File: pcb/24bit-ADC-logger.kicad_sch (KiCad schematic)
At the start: 14 parts

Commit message: feat: fill schematic title block
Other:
- company: (none) -> SA6MBO
- title: (none) -> 24bit ADC logger
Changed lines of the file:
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@@
 (kicad_sch (version 20211123) (generator eeschema)
   (paper "A4")
+  (title_block
+    (title "24bit ADC logger")
+    (date "%%date%%")
+    (rev "%%version%%")
+    (company "SA6MBO")
+  )
   (junction (at 187.96 36.83) (diameter 0) (color 0 0 0 0)
   )

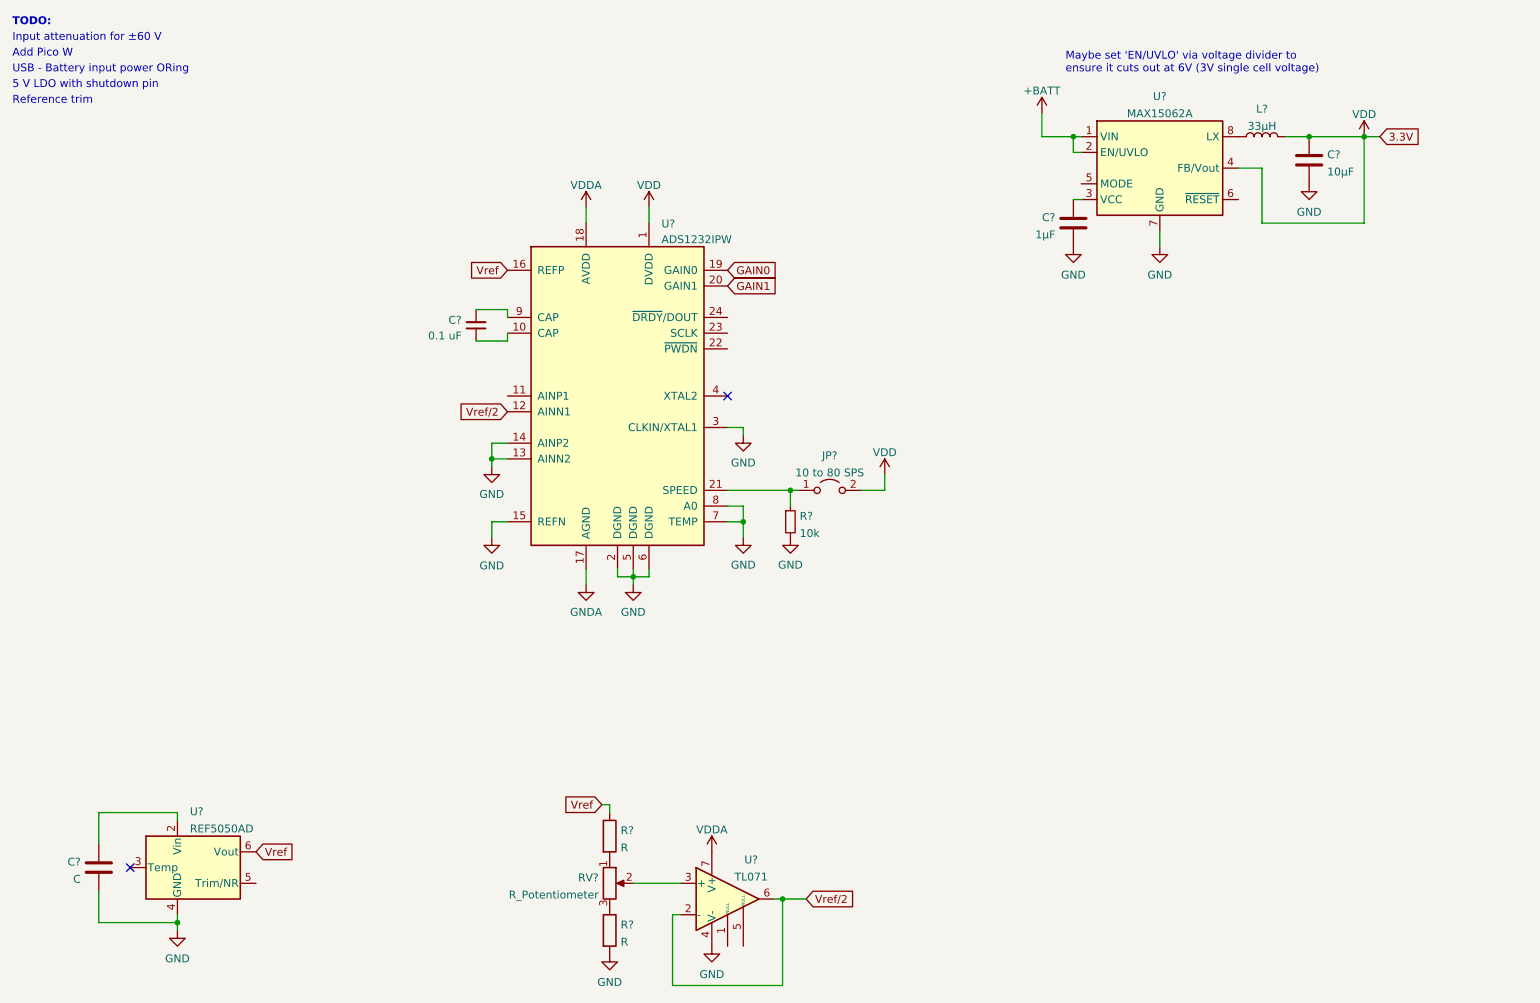
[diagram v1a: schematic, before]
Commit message: feat(sch): add battery and 5V regulator
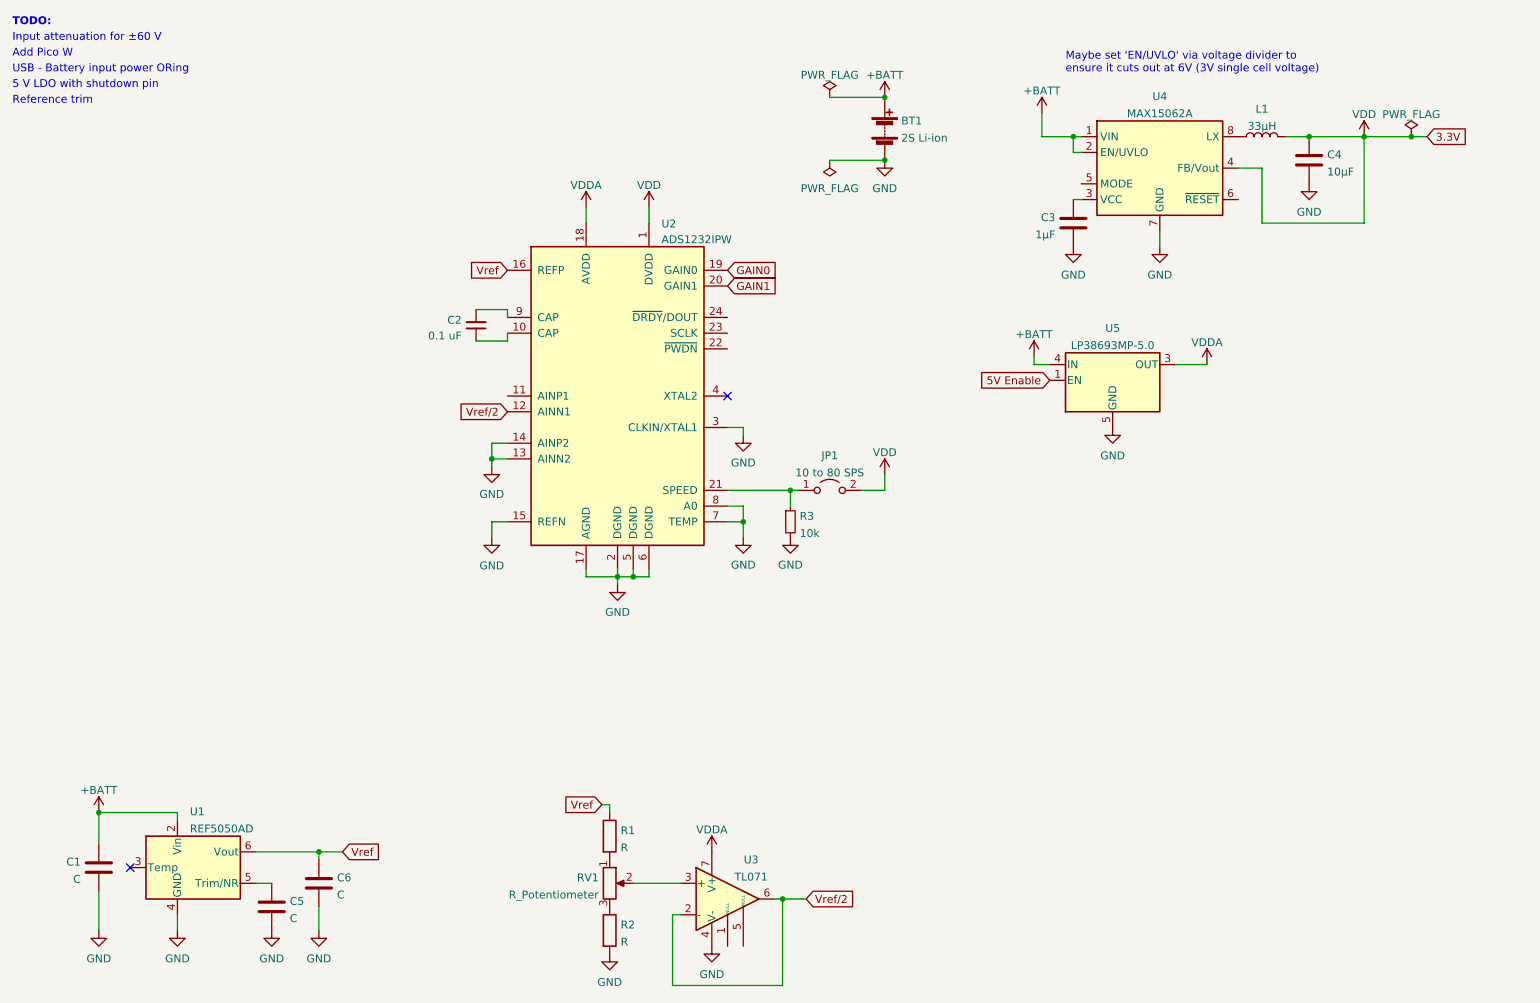
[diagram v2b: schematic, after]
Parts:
- added BT1: 2S Li-ion, symbol Device:Battery
- added C5, C6: C, symbol Device:C
- added U5: LP38693MP-5.0, Package_TO_SOT_SMD:SOT-223-5, symbol Regulator_Linear:LP38693MP-5.0
- gave numbers to parts that had none: 14
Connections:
- net GNDA is gone; now on net GND: U2.17 (AGND)
- net +BATT: now also C1.1, U1.2 (Vin), BT1.1 (+), U5.4 (IN)
- net GND: now also BT1.2 (-), C5.2, C6.2, U5.5 (GND)
- net VDDA: now also U5.3 (OUT)
- net Vref: now also C6.1
- net at U1.5 (Trim/NR): now also C5.1
- new net 5V Enable: U5.1 (EN)

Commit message: feat: add Pico W to schematic
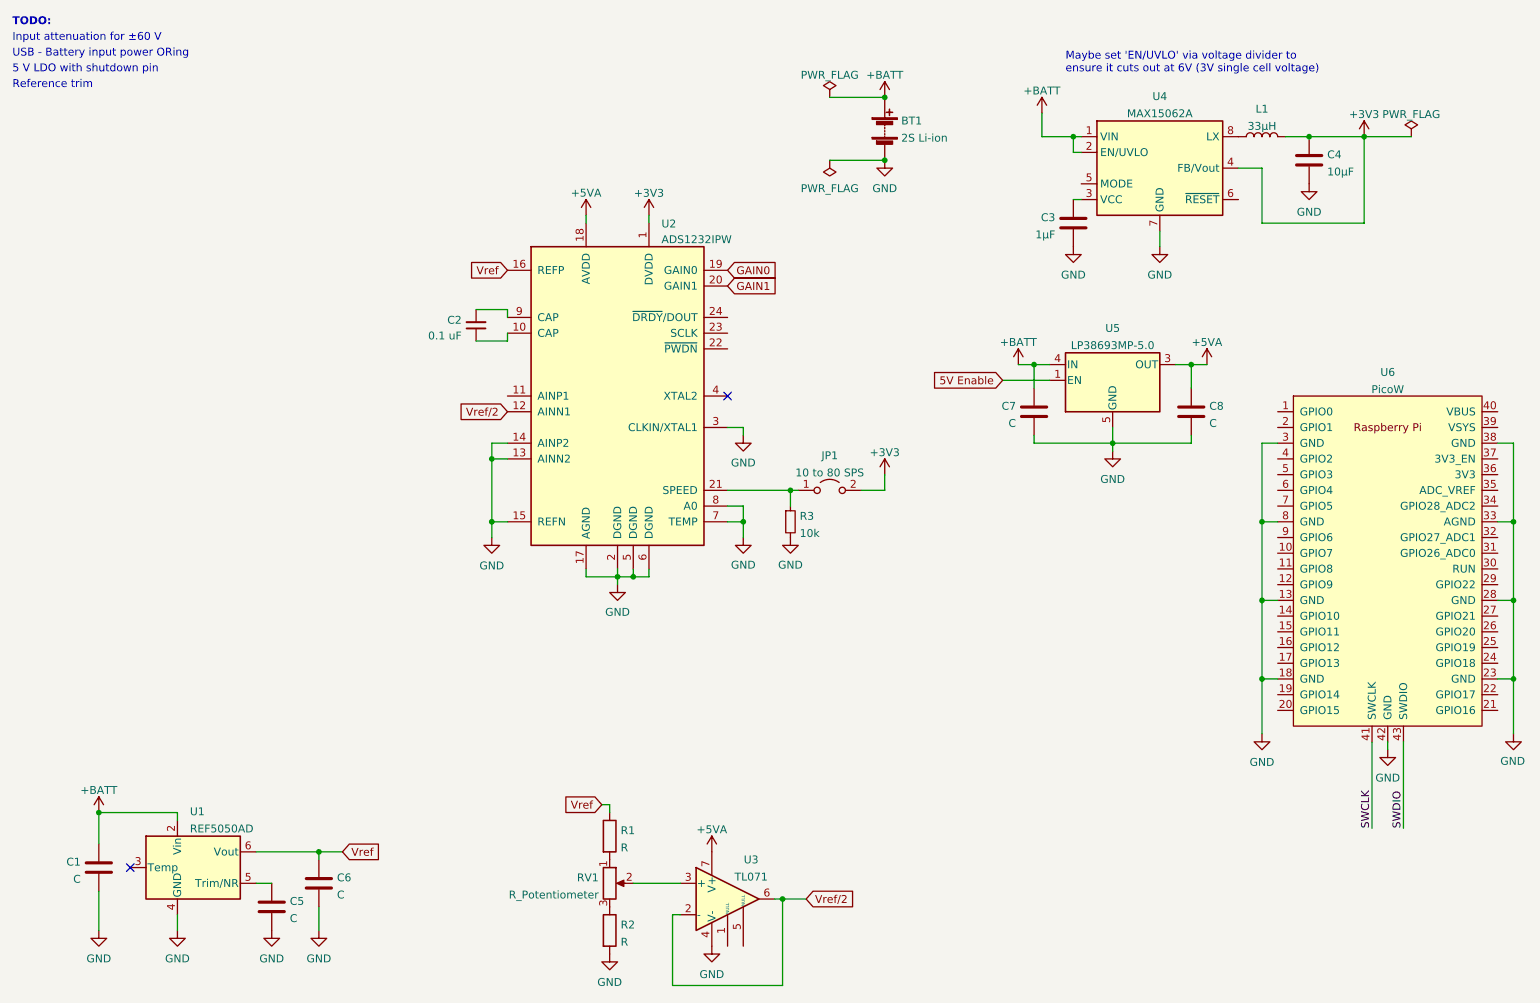
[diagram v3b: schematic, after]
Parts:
- added C7, C8: C, symbol Device:C
- added U6: PicoW, RPi_Pico:RPi_PicoW_SMD_TH, symbol RPi_Pico:PicoW
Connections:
- net +BATT: now also C7.1
- net GND: now also C7.2, C8.2, U6.13 (GND), U6.18 (GND), U6.23 (GND), U6.28 (GND), U6.3 (GND), U6.33 (AGND), U6.38 (GND), U6.42 (GND), U6.8 (GND)
- net VDD renamed +3V3
- net VDDA renamed +5VA
- net +5VA: now also C8.1
- new net SWCLK: U6.41 (SWCLK)
- new net SWDIO: U6.43 (SWDIO)
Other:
- note removed: "Add Pico W"

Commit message: test: set capacitor value to trigger CI review diff
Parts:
- C7, C8: value C -> 1uF
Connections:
- net +BATT: now also C7.2; no longer C7.1
- net GND: now also C7.1; no longer C7.2
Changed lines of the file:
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@@
     (pin "1")
   )
-  (symbol (lib_id "Device:C") (at 181.61 81.28 0) (mirror y) (unit 1)
-    (in_bom yes) (on_board yes) (fields_autoplaced)
-    (property "Reference" "C7" (id 0) (at 178.689 80.3715 0)
-      (effects (font (size 1.27 1.27)) (justify left))
-    )
-    (property "Value" "C" (id 1) (at 178.689 83.1466 0)
-      (effects (font (size 1.27 1.27)) (justify left))
-    )
-    (property "Footprint" "" (id 2) (at 180.6448 85.09 0)
+  (symbol (lib_id "Device:C") (at 181.61 81.28 0) (mirror x) (unit 1)
+    (in_bom yes) (on_board yes) (fields_autoplaced)
+    (property "Reference" "C7" (id 0) (at 178.6891 80.3715 0)
+      (effects (font (size 1.27 1.27)) (justify right))
+    )
+    (property "Value" "1uF" (id 1) (at 178.6891 83.1466 0)
+      (effects (font (size 1.27 1.27)) (justify right))
+    )
+    (property "Footprint" "" (id 2) (at 182.5752 77.47 0)
       (effects (font (size 1.27 1.27)) hide)
     )
@@
       (effects (font (size 1.27 1.27)) (justify left))
     )
-    (property "Value" "C" (id 1) (at 209.931 83.1466 0)
+    (property "Value" "1uF" (id 1) (at 209.931 83.1466 0)
       (effects (font (size 1.27 1.27)) (justify left))
     )
@@
     )
     (path "/acfc6b98-d623-44b3-b584-08e60815184f"
-      (reference "C7") (unit 1) (value "C") (footprint "")
+      (reference "C7") (unit 1) (value "1uF") (footprint "")
     )
     (path "/e08d6b8a-fd25-43ef-818b-d3ae6a475169"
-      (reference "C8") (unit 1) (value "C") (footprint "")
+      (reference "C8") (unit 1) (value "1uF") (footprint "")
     )
     (path "/5d483a2b-4b6d-4697-8bf4-fa10b54b0f95"

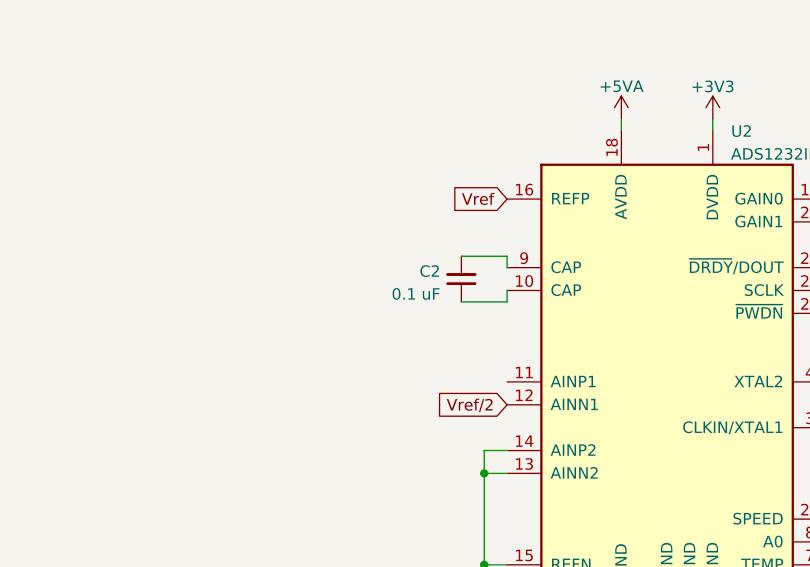
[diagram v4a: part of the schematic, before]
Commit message: ci(kibot): change commit reference for diff to HEAD~
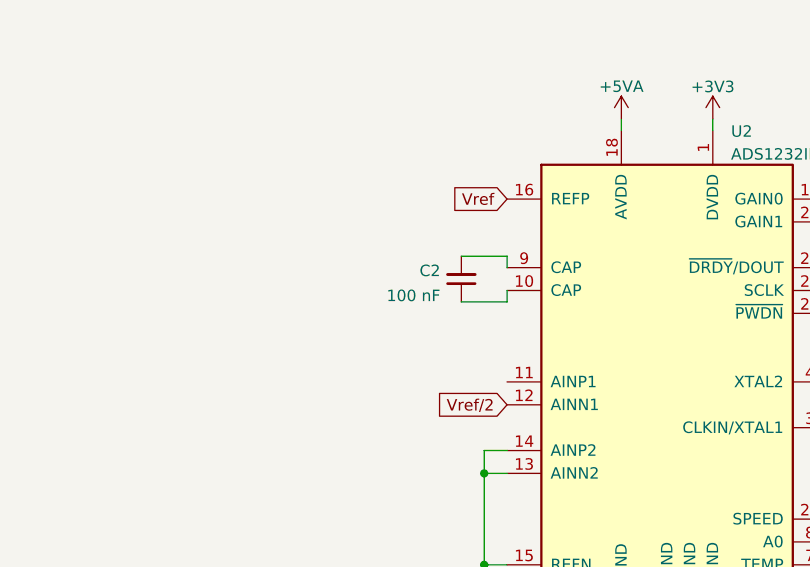
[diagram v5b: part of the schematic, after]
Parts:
- C2: value 0.1 uF -> 100 nF
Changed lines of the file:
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@@
   (symbol (lib_id "Device:C_Small") (at 91.44 67.31 0) (mirror x) (unit 1)
     (in_bom yes) (on_board yes) (fields_autoplaced)
-    (property "Reference" "C2" (id 0) (at 89.1159 66.4689 0)
+    (property "Reference" "C2" (id 0) (at 89.1159 66.3951 0)
       (effects (font (size 1.27 1.27)) (justify right))
     )
-    (property "Value" "0.1 uF" (id 1) (at 89.1159 69.0058 0)
+    (property "Value" "100 nF" (id 1) (at 89.1159 69.1702 0)
       (effects (font (size 1.27 1.27)) (justify right))
     )
@@
     )
     (path "/0fafedb4-75f0-46bd-ad25-e71605789522"
-      (reference "C2") (unit 1) (value "0.1 uF") (footprint "")
+      (reference "C2") (unit 1) (value "100 nF") (footprint "")
     )
     (path "/c2d5842f-85a0-468a-8cc5-d2ab1d5f7796"

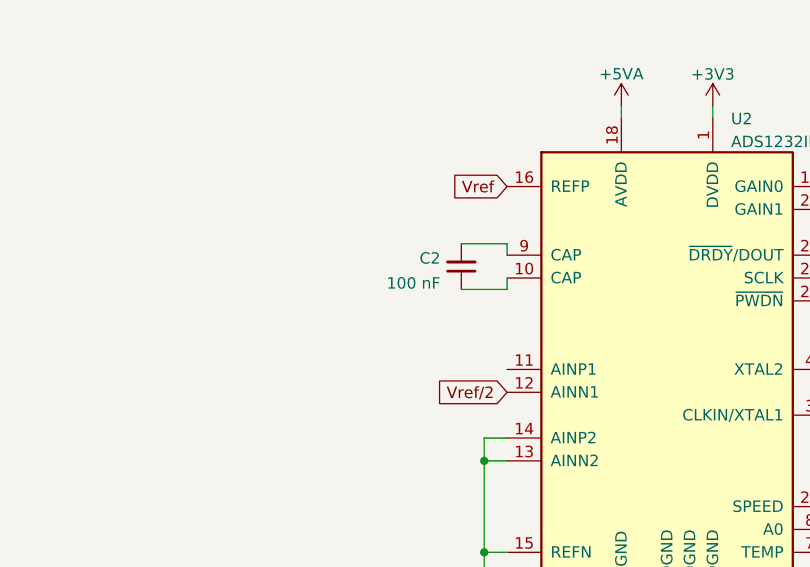
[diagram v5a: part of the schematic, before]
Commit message: test(kibot): use fixed commit hash for fault-finding
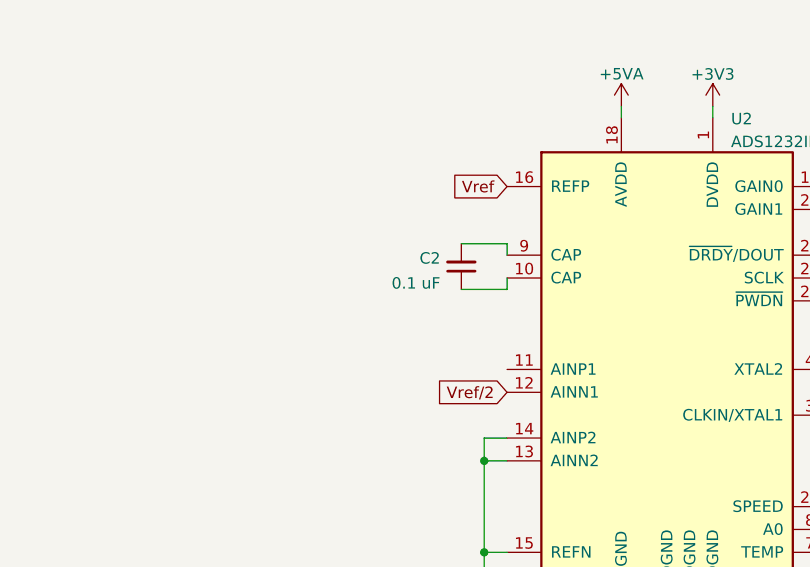
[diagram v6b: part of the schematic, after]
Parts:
- C2: value 100 nF -> 0.1 uF
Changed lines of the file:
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@@
       (effects (font (size 1.27 1.27)) (justify right))
     )
-    (property "Value" "100 nF" (id 1) (at 89.1159 69.1702 0)
+    (property "Value" "0.1 uF" (id 1) (at 89.1159 69.1702 0)
       (effects (font (size 1.27 1.27)) (justify right))
     )
@@
     )
     (path "/0fafedb4-75f0-46bd-ad25-e71605789522"
-      (reference "C2") (unit 1) (value "100 nF") (footprint "")
+      (reference "C2") (unit 1) (value "0.1 uF") (footprint "")
     )
     (path "/c2d5842f-85a0-468a-8cc5-d2ab1d5f7796"

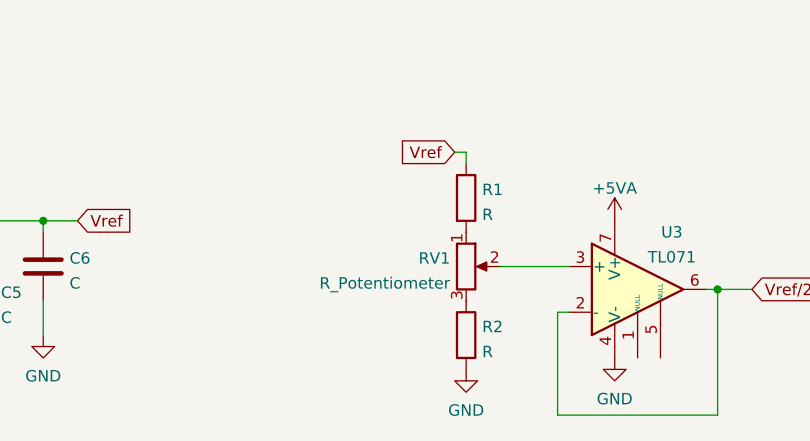
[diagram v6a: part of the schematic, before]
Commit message: fix: set values for resistor divider for vref/2
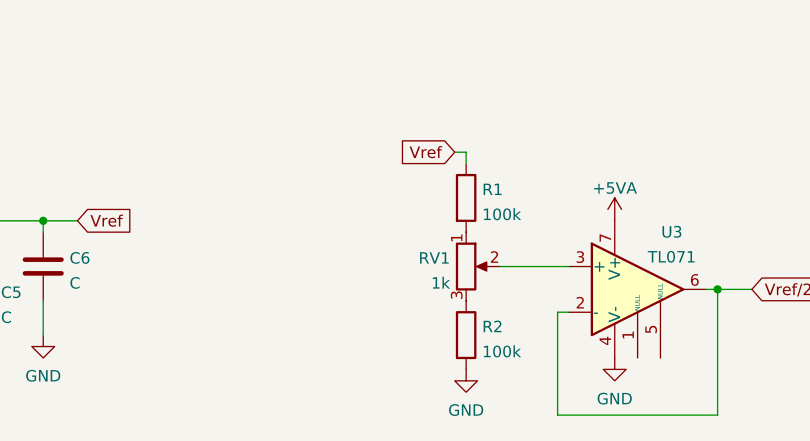
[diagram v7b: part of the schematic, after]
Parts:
- R1, R2: value R -> 100k
- RV1: value R_Potentiometer -> 1k
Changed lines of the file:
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@@
       (effects (font (size 1.27 1.27)) (justify left))
     )
-    (property "Value" "R" (id 1) (at 114.808 166.9666 0)
+    (property "Value" "100k" (id 1) (at 114.808 166.9666 0)
       (effects (font (size 1.27 1.27)) (justify left))
     )
@@
       (effects (font (size 1.27 1.27)) (justify left))
     )
-    (property "Value" "R" (id 1) (at 114.808 151.7266 0)
+    (property "Value" "100k" (id 1) (at 114.808 151.7266 0)
       (effects (font (size 1.27 1.27)) (justify left))
     )
@@
       (effects (font (size 1.27 1.27)) (justify right))
     )
-    (property "Value" "R_Potentiometer" (id 1) (at 111.2521 159.3466 0)
+    (property "Value" "1k" (id 1) (at 111.2521 159.3466 0)
       (effects (font (size 1.27 1.27)) (justify right))
     )
@@
     )
     (path "/fc245db5-421a-4183-a36a-ab38da22d07c"
-      (reference "R1") (unit 1) (value "R") (footprint "")
+      (reference "R1") (unit 1) (value "100k") (footprint "")
     )
     (path "/42757b42-27bf-4636-a81b-a0eef55159f8"
-      (reference "R2") (unit 1) (value "R") (footprint "")
+      (reference "R2") (unit 1) (value "100k") (footprint "")
     )
     (path "/f219f056-9bb7-4d30-8789-cf781989bbf6"
@@
     )
     (path "/fd82e840-dd5b-4d2f-b981-bafa8f50aca5"
-      (reference "RV1") (unit 1) (value "R_Potentiometer") (footprint "")
+      (reference "RV1") (unit 1) (value "1k") (footprint "")
     )
     (path "/b9fb1e52-5bfb-4074-afb5-c49d4199f8ba"
